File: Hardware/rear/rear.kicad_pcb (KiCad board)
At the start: 4 copper layers, 25 x 60 mm, 18 parts, among them J101 Conn_02x10_Odd_Even, J102 USB_B, J103 ARJC07-111071A, U101 AT24CS32-SSHM, U102 WE-TVS-82400102, U103 MCP3021

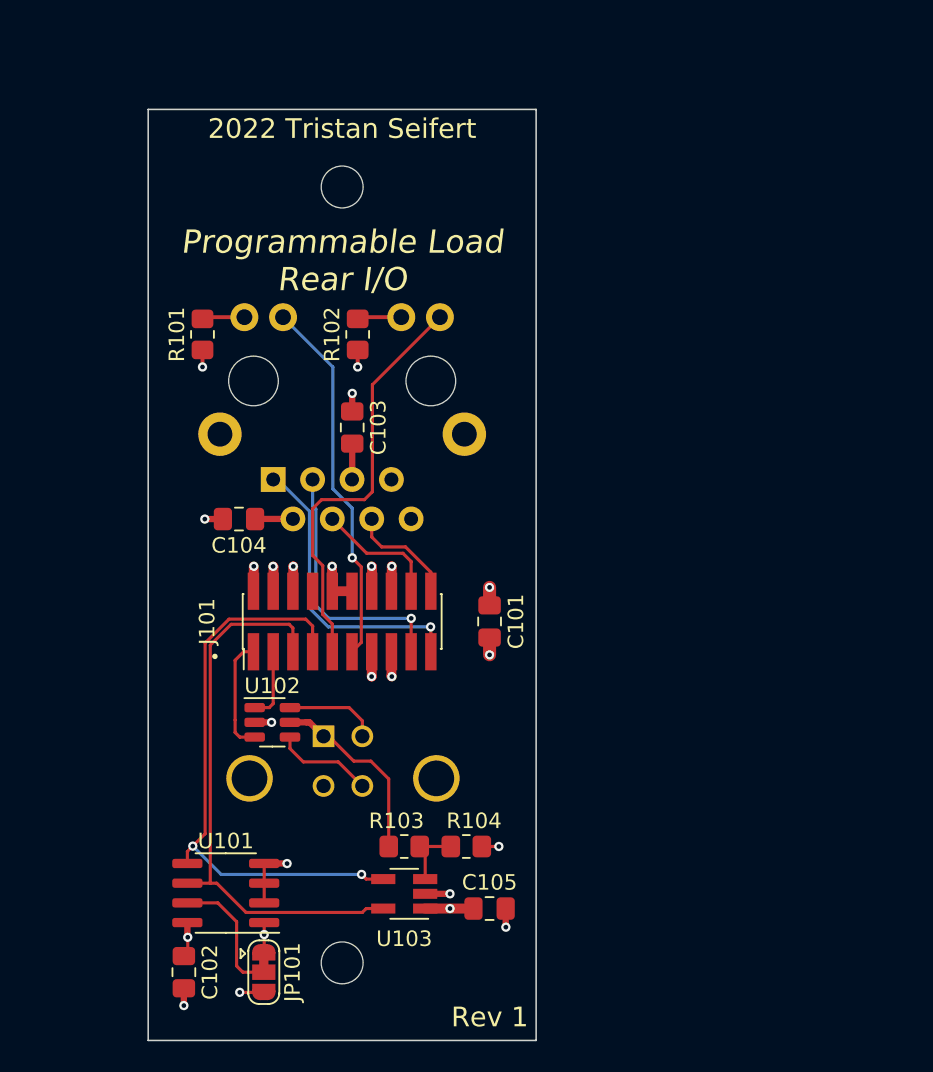
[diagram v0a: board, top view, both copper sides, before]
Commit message: Re-design around STM32MP1 (#2)
* Start work on rev3 hardware

- This fits the Technomet R110 enclosure and supports multiple load
  boards, connected via CAN rather than I2C. Each load has a
  microcontroller of its own.

* More new layout stuff

- More work on the new controller board layout

- Rework rear IO board for the new Technomet rear panel (it has an
  expansion connector for CAN also, and features four screw holes
  instead of two)

- Added a few footprints (expansion RJ45 connector; some
  horizontal/vertical headers)

* Work on controller VSense, power

- Routed 3V3 switching supply

- Created footprint and symbols for Kemet EA2 series latching relay

- Added relays to controller to handle routing of voltage sense inputs
  to the sampling ADC

* Rear IO rework

- Mostly finished the rear IO board rework (adding the CAN filtering and
  switchable termination; trigger input pulse shaper; fuses for
  expansion +12V)

- Changed encoder type on front panel for a shorter type

- Created schematic models and footprints for Bournds DR311 chokes;
  Mill-Max 2108 solder turrets

* More work on new controller board

- Switched mains connection for a push-in screw terminal, rather than a
  pluggable block (takes up less space, less parts)

- Added input terminal for rear VSense inputs

- Added -5V supply (same circuit as on analog board; required for
  voltage input sense)

- Replaced beeper with a side-firing version. It takes up a bunch less
  space vertically, and also now added a resistor to (hopefully) make it
  somewhat more quiet

- Added connector for bonus displays

* Add "bonus display" board

- Created the bonus display board, which houses a chip-on-glass 4x10
  text character display. It's meant to be mounted next to the input
  jacks to show a constant location of current/voltage, even if the main
  display is used for menus or other stuff.

- More tweaks to controller board, to do with power g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
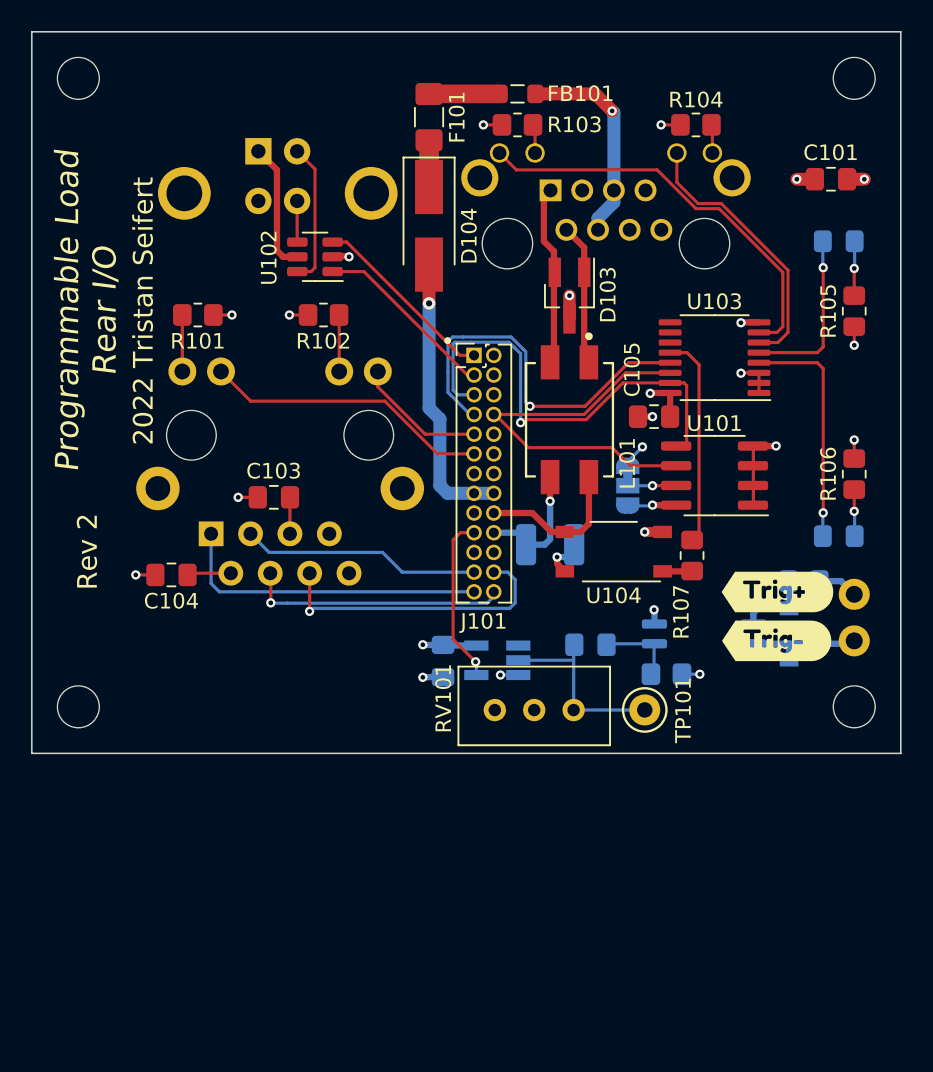
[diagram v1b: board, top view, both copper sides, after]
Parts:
- added C106: 100nF, Capacitor_SMD:C_0805_2012Metric_Pad1.18x1.45mm_HandSolder, B.Cu at (46.5, 60.5)
- added D101: Green, LED_SMD:LED_0805_2012Metric_Pad1.15x1.40mm_HandSolder, B.Cu at (72.0, 33.5)
- added D102: Green, LED_SMD:LED_0805_2012Metric_Pad1.15x1.40mm_HandSolder, B.Cu at (72.0, 52.5)
- added D103: ESDONCAN1, Package_TO_SOT_SMD:SOT-23_Handsoldering, F.Cu at (54.6, 37.0)
- added D104: Panjit SS14, Diode_SMD:D_SMA_Handsoldering, F.Cu at (45.6, 32.5)
- added D105: 1N4148W, Diode_SMD:D_SOD-123, B.Cu at (68.8, 58.8)
- added F101: 500mA, Fuse:Fuse_1206_3216Metric_Pad1.42x1.75mm_HandSolder, F.Cu at (45.6, 25.5)
- added FB101: FerriteBead_Small, Inductor_SMD:L_0805_2012Metric_Pad1.05x1.20mm_HandSolder, F.Cu at (51.3, 24.0)
- added H103: MountingHole, MountingHole:MountingHole_2.7mm_M2.5, F.Cu at (73.0, 63.5)
- added H104: MountingHole, MountingHole:MountingHole_2.7mm_M2.5, F.Cu at (23.0, 63.5)
- added J104: CRJ061-L1-TH, programmable-load:CUI_CRJ061-L1-TH, B.Cu at (57.0, 33.6)
- added J105: Conn_01x01, programmable-load:MillMax-2108-2, F.Cu at (73.0, 56.2)
- added J106: Conn_01x01, programmable-load:MillMax-2108-2, F.Cu at (73.0, 59.2)
- added L101: DR331-513BE, programmable-load:Bourns-DR331-0-0-MFG, F.Cu at (54.6, 45.0)
- added R105: 1k, Resistor_SMD:R_0805_2012Metric_Pad1.20x1.40mm_HandSolder, F.Cu at (73.0, 38.0)
- added R106: 1k, Resistor_SMD:R_0805_2012Metric_Pad1.20x1.40mm_HandSolder, F.Cu at (73.0, 48.5)
- added R107: 1k, Resistor_SMD:R_0805_2012Metric_Pad1.20x1.40mm_HandSolder, F.Cu at (62.5, 53.8)
- added R108: 100R, Resistor_SMD:R_1210_3225Metric_Pad1.30x2.65mm_HandSolder, B.Cu at (53.4, 53.0)
- added R109: 200R, Resistor_SMD:R_0805_2012Metric_Pad1.20x1.40mm_HandSolder, B.Cu at (69.8, 55.4)
- added R110: 47k, Resistor_SMD:R_0805_2012Metric_Pad1.20x1.40mm_HandSolder, B.Cu at (60.9, 61.4)
- added RV101: 500k, programmable-load:Potentiometer_Nidec_Copal_CT94EW, F.Cu at (57.4, 66.0)
- added TP101: Trigger, TestPoint:TestPoint_Keystone_5000-5004_Miniature, F.Cu at (59.5, 63.7)
- added U104: TLP170A, Package_SO:MFSOP6-4_4.4x3.6mm_P1.27mm, F.Cu at (57.5, 53.5)
- added U105: FODM217B, Package_SO:SOP-4_4.4x2.6mm_P1.27mm, B.Cu at (63.3, 58.8)
- added U106: 74LVC1G17, Package_TO_SOT_SMD:SOT-23-5_HandSoldering, B.Cu at (50.0, 60.5)
- added kibuzzard-62664110: G***, kibuzzard-62664110, F.Cu at (68.0, 59.2)
- added kibuzzard-62664123: G***, kibuzzard-62664123, F.Cu at (68.0, 56.1)
- C102: value 100nF -> 1µF; moved to B.Cu
- J101: footprint Connector_PinHeader_1.27mm:PinHeader_2x10_P1.27mm_Vertical_SMD -> Connector_PinHeader_1.27mm:PinHeader_2x13_P1.27mm_Vertical
- JP101: moved to B.Cu
- R103: value 7k5 -> 100R
- R104: value 12k -> 100R
- U103: value MCP3021 -> XRA1200; footprint Package_TO_SOT_SMD:SOT-23-5_HandSoldering -> Package_SO:TSSOP-16_4.4x5mm_P0.65mm
- moved H102 65.9 mm to (73.0, 23.0)
- moved R104 48.8 mm to (62.8, 26.0), turned to 180 degrees
- moved R103 47.1 mm to (51.3, 26.0), turned to 180 degrees
- moved U101 41.4 mm to (64.0, 48.6)
- moved U103 39.9 mm to (64.0, 41.0)
- moved JP101 39.2 mm to (58.4, 49.2)
- moved J102 37.9 mm to (34.6, 27.7)
- moved C101 36.0 mm to (71.5, 29.5), turned to 180 degrees
- moved C102 33.6 mm to (56.0, 59.5), turned to 0 degrees
- moved C105 33.4 mm to (60.1, 44.8), turned to 180 degrees
- moved U102 30.1 mm to (38.2, 34.5), turned to 180 degrees
- moved J101 19.1 mm to (48.5, 40.9), turned to 0 degrees
- moved H101 18.4 mm to (23.0, 23.0)
- moved C103 6.76 mm to (35.6, 50.0), turned to 0 degrees
- moved C104 5.65 mm to (29.0, 55.0)
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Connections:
- C102 pad 1: +3V3 -> Net-(C102-Pad1)
- C102 pad 2: GND -> Net-(U105-Pad3)
- J101 pad 15: GND -> +12V
- J101 pad 16: GND -> +12V
- J101 pad 17: /ETH_TX- -> GND
- J101 pad 18: /ETH_RX+ -> /CANL
- J101 pad 19: /ETH_TX+ -> /TRIGGER
- J101 pad 20: /ETH_RX- -> /CANH
- J101 pad 5: /SCL -> /SDA
- J101 pad 7: /SDA -> /~{IRQ}
- J101 pad 8: /~{IRQ} -> /SCL
- R103 pad 1: VBUS -> Net-(J104-Pad10)
- R103 pad 2: Net-(R103-Pad2) -> +3V3
- R104 pad 1: Net-(R103-Pad2) -> Net-(J104-Pad12)
- R104 pad 2: GND -> +3V3
- U103 pad 1: +3V3 -> GND
- U103 pad 3: Net-(R103-Pad2) -> GND
- U103 pad 4: /SDA -> /~{LED_TRIGGER}
- U103 pad 5: /SCL -> /~{LED_VSENSE}
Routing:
- net /~{EXT_LED0}: track 0.00 -> 26.6 mm
- net /~{IRQ}: track 0.00 -> 24.9 mm, vias 0 -> 1
- net /ETH_LED1: track 27.1 -> 8.46 mm
- net +12V: track 0.00 -> 18.2 mm, vias 0 -> 1
- net /~{EXT_LED1}: track 0.00 -> 17.5 mm
- net /~{LED_TRIGGER}: track 0.00 -> 15.1 mm, vias 0 -> 1
- net /TERM_EN: track 0.00 -> 13.7 mm
- net Net-(FB101-Pad1): track 0.00 -> 13.5 mm, vias 0 -> 1
- net Net-(C102-Pad1): track 0.00 -> 12.4 mm
- net Net-(D103-Pad2): track 0.00 -> 12.2 mm
- net /ETH_RX-: track 7.14 -> 18.7 mm, vias 0 -> 1
- net /~{LED_VSENSE}: track 0.00 -> 11.1 mm, vias 0 -> 1
- net /TRIGGER: track 0.00 -> 10.9 mm, vias 0 -> 1
- net /SCL: track 36.4 -> 25.6 mm
- net /CANL: track 0.00 -> 9.85 mm
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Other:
- board size 25 x 60 mm -> 56 x 46.5 mm
- board text added: "Rev 2"
- board text removed: "Rev 1"
